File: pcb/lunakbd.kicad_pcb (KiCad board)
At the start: 2 copper layers, 134.4 x 112.7 mm, 72 parts, among them J1 TRRS-PJ-320D, J2 Battery_Socket, J3 Conn_Display, SW1 Switch, SW10 Switch, SW11 Switch, SW12 Switch, SW13 Switch, SW14 Switch, SW15 Switch, SW16 Switch, SW17 Switch, SW18 Switch, SW19 Switch, SW2 Switch, SW20 Switch, SW21 Switch, SW22 Switch, SW23 Switch, SW24 Switch, SW25 Switch, SW26 Switch, SW27 Switch, SW28 Switch, SW29 RotaryEncoder_SW, SW3 Switch, SW30 Reset_Button, SW31 Battery_Switch, SW4 Switch, SW5 Switch, SW6 Switch, SW7 Switch, SW8 Switch, SW9 Switch, U1 ProMicro

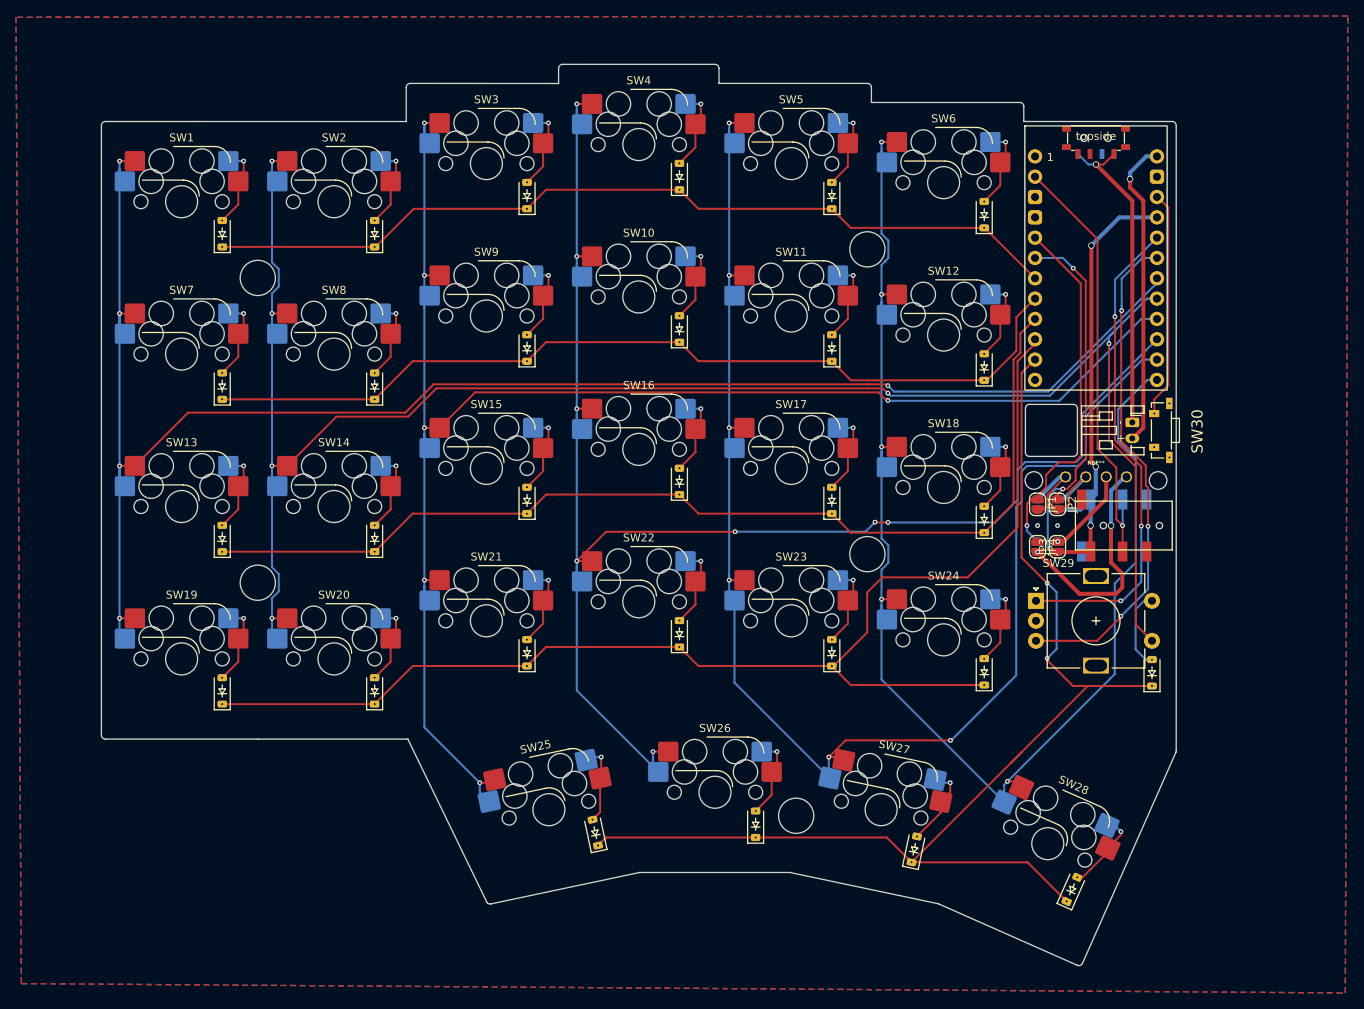
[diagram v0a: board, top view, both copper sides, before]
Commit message: refactor: update all footprints and fix thumb keys align
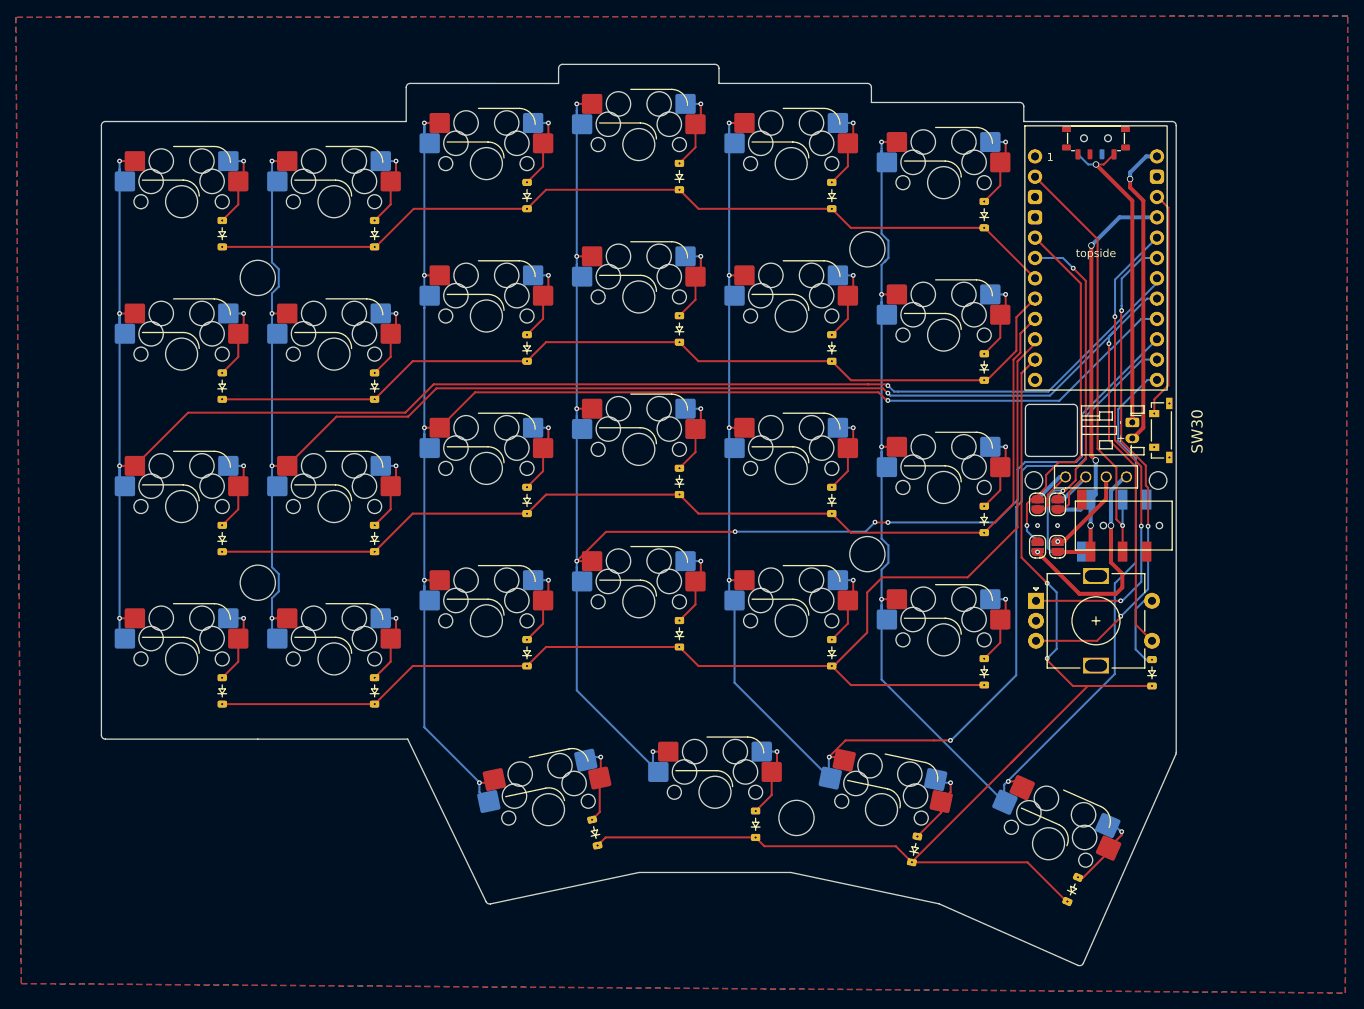
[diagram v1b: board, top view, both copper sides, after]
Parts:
- D1, D10, D11, D12, D13, D14, D15, D16, D17, D18, D19, D2, D20, D21, D22, D23, D24, D25, D26, D27, D28, D29, D3, D4, D5, D6, D7, D8, D9: footprint Library:D_SOD-123 -> lunalib:D_SOD-123
- J2: footprint Connector_JST:JST_PH_S2B-PH-K_1x02_P2.00mm_Horizontal -> lunalib:JST_PH_S2B-PH-K_1x02_P2.00mm_Horizontal
- J3: footprint kbd:OLED -> lunalib:OLED
- JP1, JP2, JP3, JP4, JP5, JP6, JP7, JP8: footprint Jumper:SolderJumper-2_P1.3mm_Open_RoundedPad1.0x1.5mm -> lunalib:SolderJumper-2_P1.3mm_Open_RoundedPad1.0x1.5mm
- SW1, SW10, SW11, SW12, SW13, SW14, SW15, SW16, SW17, SW18, SW19, SW2, SW20, SW21, SW22, SW23, SW24, SW25, SW26, SW27, SW3, SW4, SW5, SW6, SW7, SW8, SW9: footprint Library:SW_Hotswap_Kailh_MX_1.00u -> lunalib:SW_Hotswap_Kailh_MX_1.00u
- SW28: footprint Library:SW_Hotswap_Kailh_MX_1.25u_90deg -> lunalib:SW_Hotswap_Kailh_MX_1.25u_90deg
- SW29: footprint Rotary_Encoder:RotaryEncoder_Alps_EC11E-Switch_Vertical_H20mm -> lunalib:RotaryEncoder_Alps_EC11E-Switch_Vertical_H20mm
- SW30: footprint Library:SW_TL3330AF130QG -> lunalib:SW_TL3330AF130QG
- SW31: footprint Library:SW_MSK12C02-HB -> lunalib:SW_MSK12C02-HB
- U1: footprint PCM_marbastlib-xp-promicroish:SuperMini_nRF52840_H_USBup -> lunalib:SuperMini_nRF52840
- moved D28 0.10 mm to (187.6, 138.4)
- moved SW28 0.10 mm to (184.6, 132.6)
- moved D25 0.05 mm to (127.9, 131.2)
- moved SW25 0.05 mm to (122.1, 128.4)
- moved SW27 0.05 mm to (163.7, 128.4)
- moved D27 0.05 mm to (167.8, 133.3)
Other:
- outline, holes or cut-outs redrawn

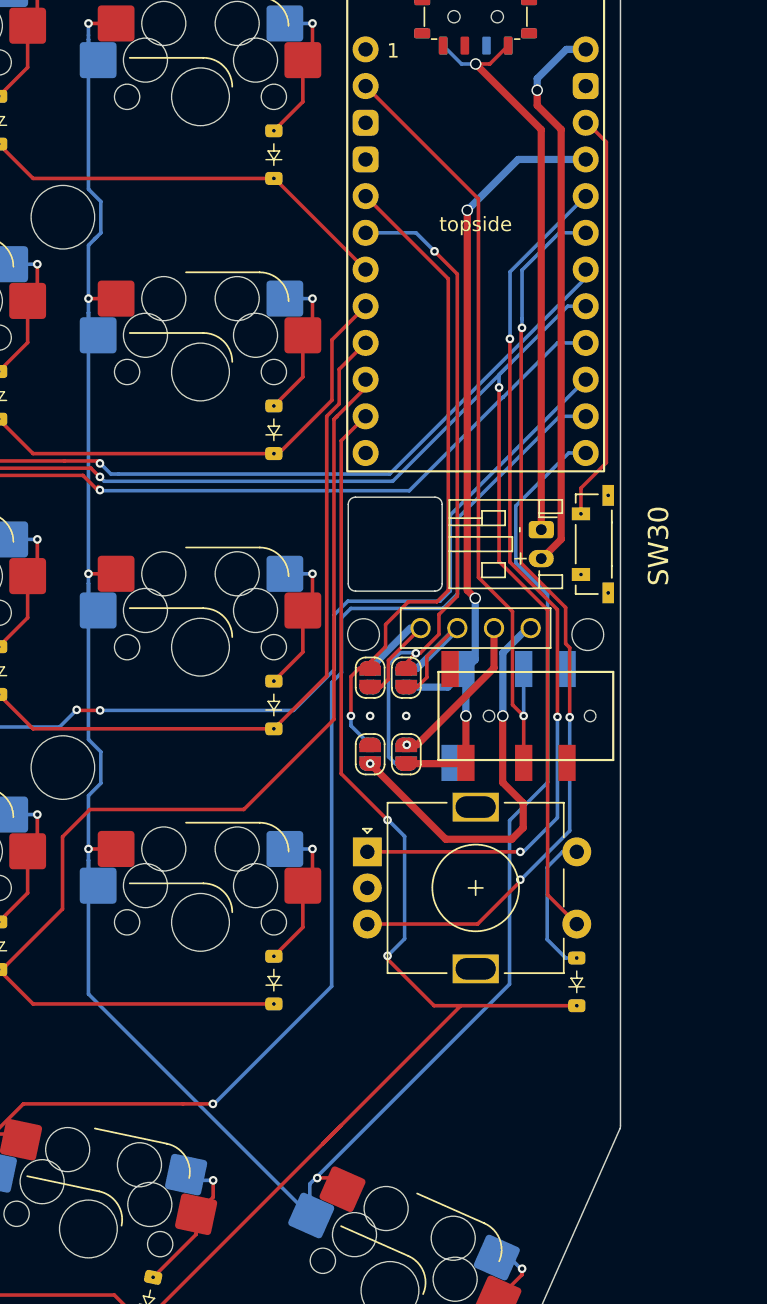
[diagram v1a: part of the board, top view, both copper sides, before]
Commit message: fix: reset button footprint
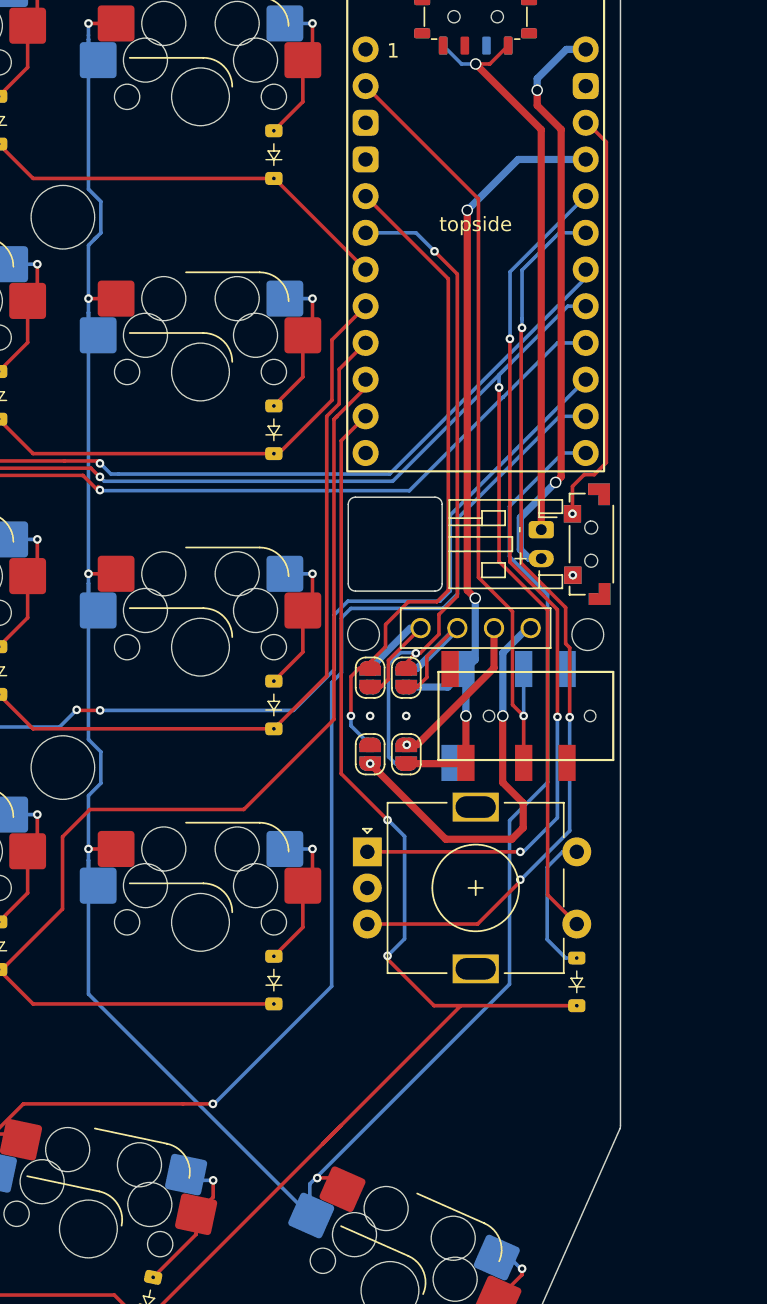
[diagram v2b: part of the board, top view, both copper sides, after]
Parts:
- J1: footprint Library:TRRS-PJ-320D -> lunalib:TRRS-PJ-320D
- SW30: footprint lunalib:SW_TL3330AF130QG -> lunalib:SW-RESET_BTN
- moved SW30 0.54 mm to (198.1, 81.0)
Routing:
- net B+: track 39.3 -> 41.0 mm, vias 1 -> 2
- net reset: track 28.4 -> 29.1 mm, vias 0 -> 1
- net col-5: track 171.2 -> 171.8 mm
- net GND: vias 2 -> 3

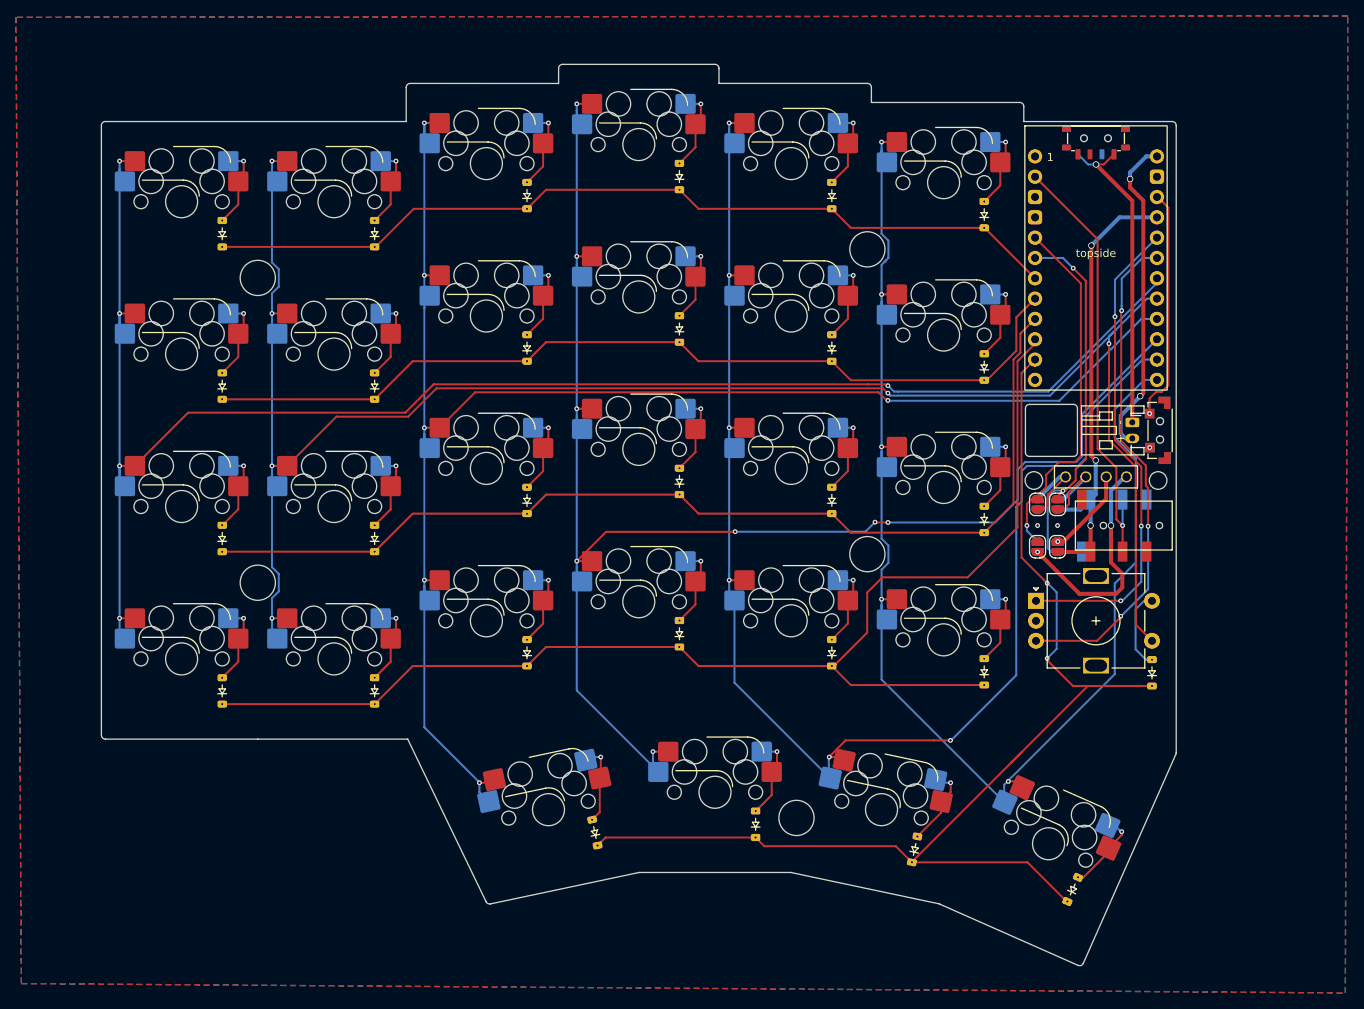
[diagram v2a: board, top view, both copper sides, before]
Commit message: fix: clearence errors
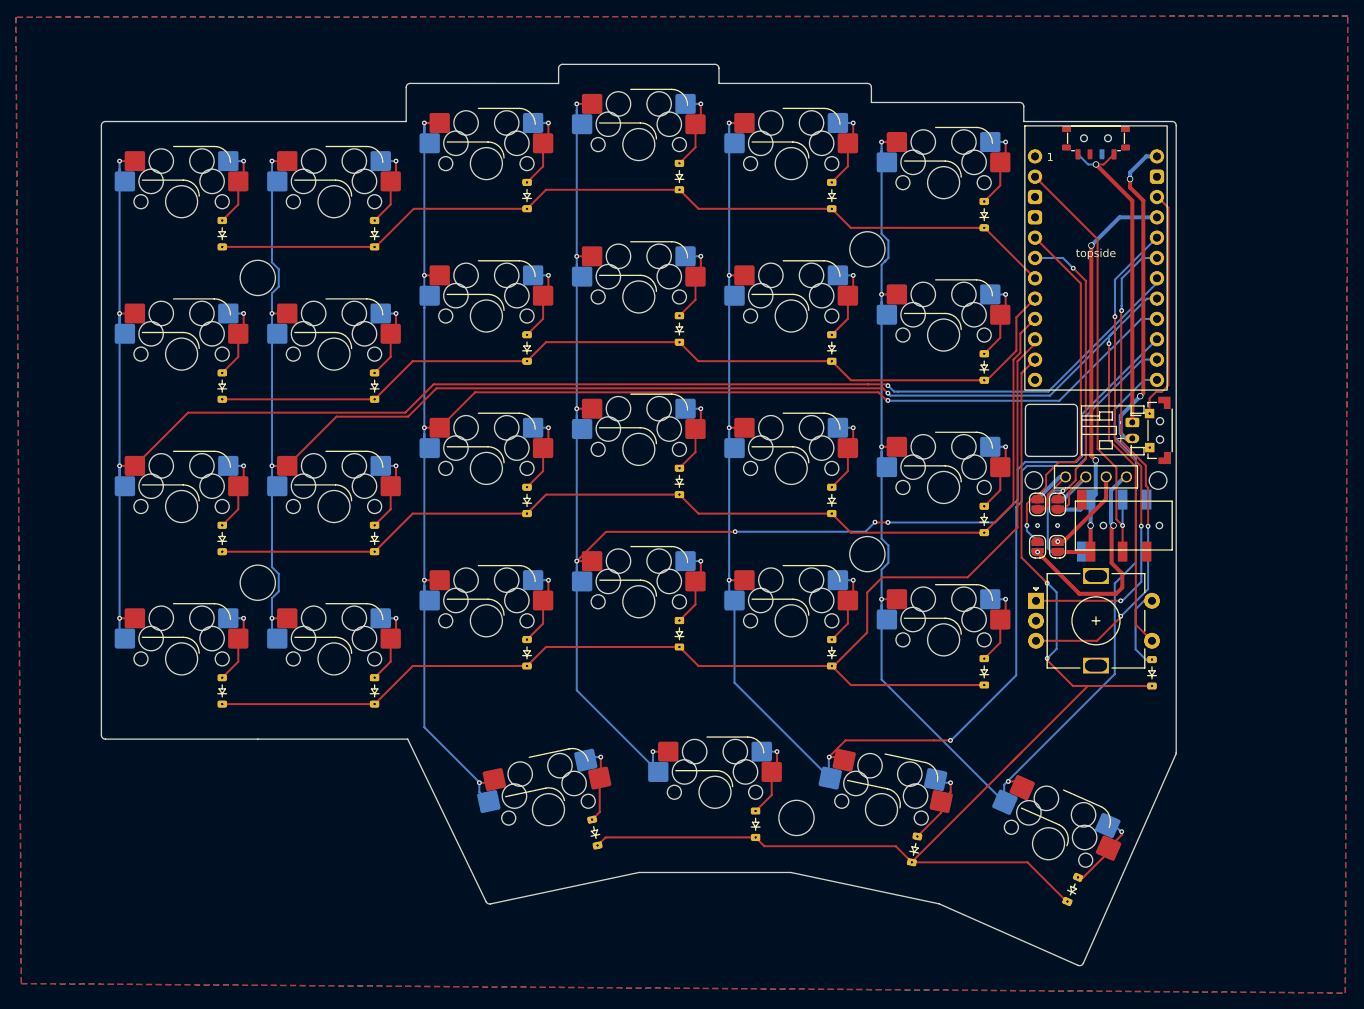
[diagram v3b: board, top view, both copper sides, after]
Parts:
- SW30: footprint lunalib:SW-RESET_BTN -> lunalib:SW-SMD_SHOU_TS36CA-0.6
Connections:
- SW30 pad 1: GND -> reset
- SW30 pad 2: reset -> GND
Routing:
- net reset: vias 1 -> 0
- net GND: vias 3 -> 2

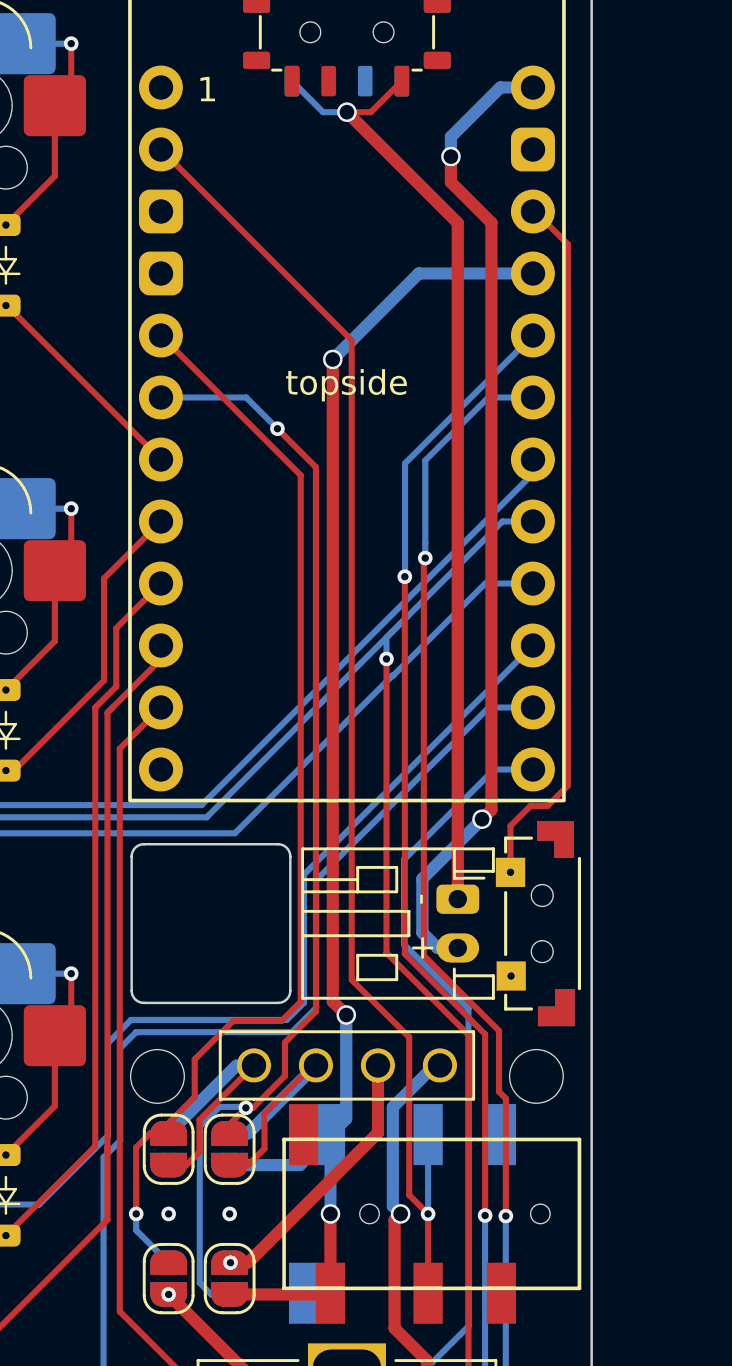
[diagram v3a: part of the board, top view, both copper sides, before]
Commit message: feat: add logo silkscreen
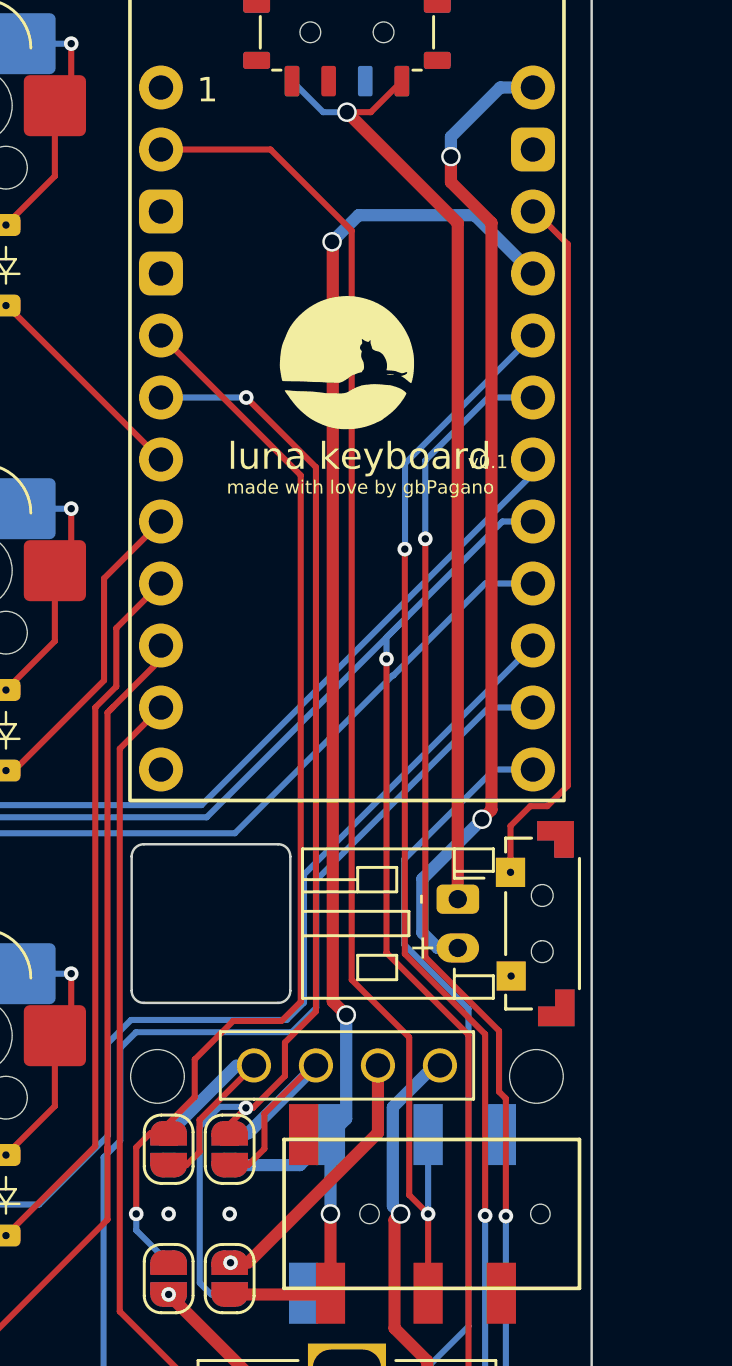
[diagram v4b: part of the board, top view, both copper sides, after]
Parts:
- added G***: LOGO, Library:test3, F.Cu at (190.5, 58.0)
- added G***: LOGO, Library:test3, B.Cu at (190.5, 58.0)
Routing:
- net VCC: track 58.0 -> 62.9 mm
- net data: track 54.6 -> 57.3 mm
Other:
- board text added: "luna keyboard"
- board text added: "made with love by gbPagano"
- board text added: "v0.1"
